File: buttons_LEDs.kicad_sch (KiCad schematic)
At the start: 6 parts, among them SW1 SW_Push, SW2 SW_Push

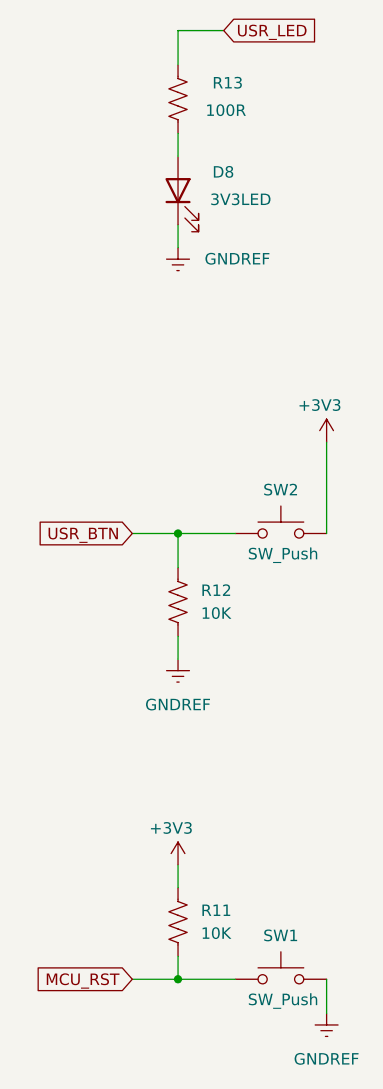
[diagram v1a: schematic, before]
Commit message: Completed design for digital outputs, tidied into own sheets and bussing for scalability
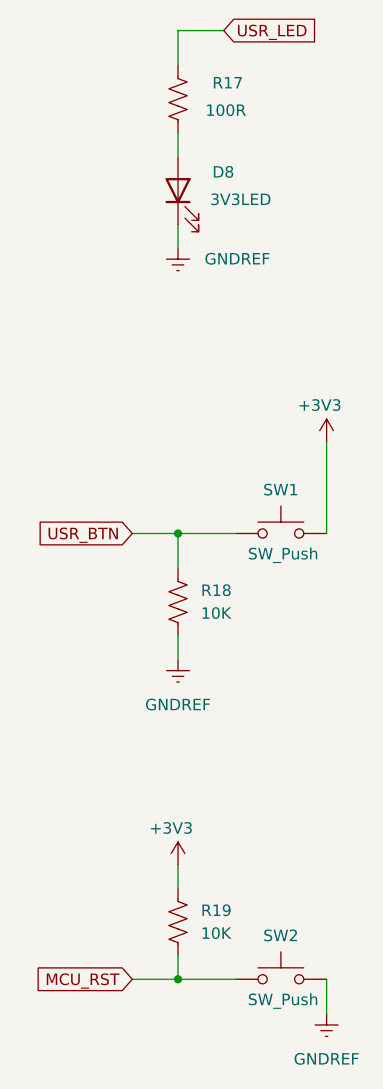
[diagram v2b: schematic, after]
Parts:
- renumbered R13 to R17, R12 to R18, R11 to R19, SW2 to SW1, SW1 to SW2
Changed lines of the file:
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@@
 		(on_board yes)
 		(dnp no)
-		(property "Reference" "#PWR0146"
+		(property "Reference" "#PWR0127"
 			(at 124.46 120.65 0)
 			(effects
@@
 			(project "Remora Nucleo F446ZE Hat"
 				(path "/5473abc6-7b93-43cc-a401-f691c4d7d7cf/e0f94f66-f67a-46dc-b55b-a3f70607aba8"
-					(reference "#PWR0146")
+					(reference "#PWR0127")
 					(unit 1)
 				)
@@
 		(on_board yes)
 		(dnp no)
-		(property "Reference" "SW2"
+		(property "Reference" "SW1"
 			(at 135.89 75.184 0)
 			(effects
@@
 			(project "Remora Nucleo F446ZE Hat"
 				(path "/5473abc6-7b93-43cc-a401-f691c4d7d7cf/e0f94f66-f67a-46dc-b55b-a3f70607aba8"
-					(reference "SW2")
+					(reference "SW1")
 					(unit 1)
 				)
@@
 		(dnp no)
 		(fields_autoplaced yes)
-		(property "Reference" "#PWR0149"
+		(property "Reference" "#PWR0126"
 			(at 124.46 100.33 0)
 			(effects
@@
 			(project "Remora Nucleo F446ZE Hat"
 				(path "/5473abc6-7b93-43cc-a401-f691c4d7d7cf/e0f94f66-f67a-46dc-b55b-a3f70607aba8"
-					(reference "#PWR0149")
+					(reference "#PWR0126")
 					(unit 1)
 				)
@@
 		(dnp no)
 		(fields_autoplaced yes)
-		(property "Reference" "R12"
+		(property "Reference" "R18"
 			(at 127 86.3599 0)
 			(effects
@@
 			(project "Remora Nucleo F446ZE Hat"
 				(path "/5473abc6-7b93-43cc-a401-f691c4d7d7cf/e0f94f66-f67a-46dc-b55b-a3f70607aba8"
-					(reference "R12")
+					(reference "R18")
 					(unit 1)
 				)
@@
 		(on_board yes)
 		(dnp no)
-		(property "Reference" "#PWR0148"
+		(property "Reference" "#PWR0128"
 			(at 140.97 73.66 0)
 			(effects
@@
 			(project "Remora Nucleo F446ZE Hat"
 				(path "/5473abc6-7b93-43cc-a401-f691c4d7d7cf/e0f94f66-f67a-46dc-b55b-a3f70607aba8"
-					(reference "#PWR0148")
+					(reference "#PWR0128")
 					(unit 1)
 				)
@@
 		(on_board yes)
 		(dnp no)
-		(property "Reference" "#PWR0151"
+		(property "Reference" "#PWR0125"
 			(at 124.46 54.61 0)
 			(effects
@@
 			(project "Remora Nucleo F446ZE Hat"
 				(path "/5473abc6-7b93-43cc-a401-f691c4d7d7cf/e0f94f66-f67a-46dc-b55b-a3f70607aba8"
-					(reference "#PWR0151")
+					(reference "#PWR0125")
 					(unit 1)
 				)
@@
 		(on_board yes)
 		(dnp no)
-		(property "Reference" "R13"
+		(property "Reference" "R17"
 			(at 128.27 29.972 0)
 			(effects
@@
 			(project "Remora Nucleo F446ZE Hat"
 				(path "/5473abc6-7b93-43cc-a401-f691c4d7d7cf/e0f94f66-f67a-46dc-b55b-a3f70607aba8"
-					(reference "R13")
+					(reference "R17")
 					(unit 1)
 				)
@@
 		(dnp no)
 		(fields_autoplaced yes)
-		(property "Reference" "R11"
+		(property "Reference" "R19"
 			(at 127 121.9199 0)
 			(effects
@@
 			(project "Remora Nucleo F446ZE Hat"
 				(path "/5473abc6-7b93-43cc-a401-f691c4d7d7cf/e0f94f66-f67a-46dc-b55b-a3f70607aba8"
-					(reference "R11")
+					(reference "R19")
 					(unit 1)
 				)
@@
 		(on_board yes)
 		(dnp no)
-		(property "Reference" "SW1"
+		(property "Reference" "SW2"
 			(at 135.89 124.714 0)
 			(effects
@@
 			(project "Remora Nucleo F446ZE Hat"
 				(path "/5473abc6-7b93-43cc-a401-f691c4d7d7cf/e0f94f66-f67a-46dc-b55b-a3f70607aba8"
-					(reference "SW1")
+					(reference "SW2")
 					(unit 1)
 				)
@@
 		(dnp no)
 		(fields_autoplaced yes)
-		(property "Reference" "#PWR0147"
+		(property "Reference" "#PWR0129"
 			(at 140.97 139.7 0)
 			(effects
@@
 			(project "Remora Nucleo F446ZE Hat"
 				(path "/5473abc6-7b93-43cc-a401-f691c4d7d7cf/e0f94f66-f67a-46dc-b55b-a3f70607aba8"
-					(reference "#PWR0147")
-					(unit 1)
-				)
+					(reference "#PWR0129")
+					(unit 1)
+				)

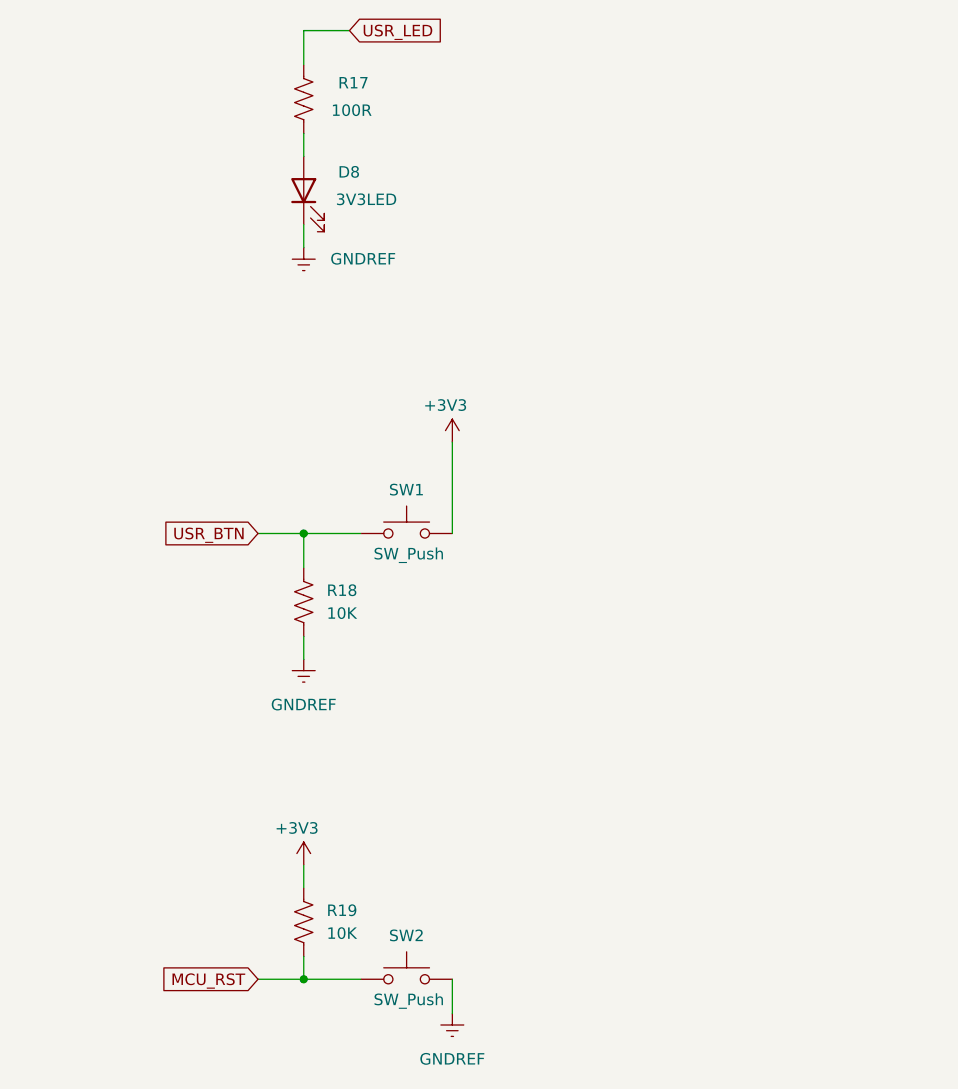
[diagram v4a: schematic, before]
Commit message: Fixed bug with lack of pin header for CN11 and CN12. Addeded RPI header and aligned it, assigned some safe footprints
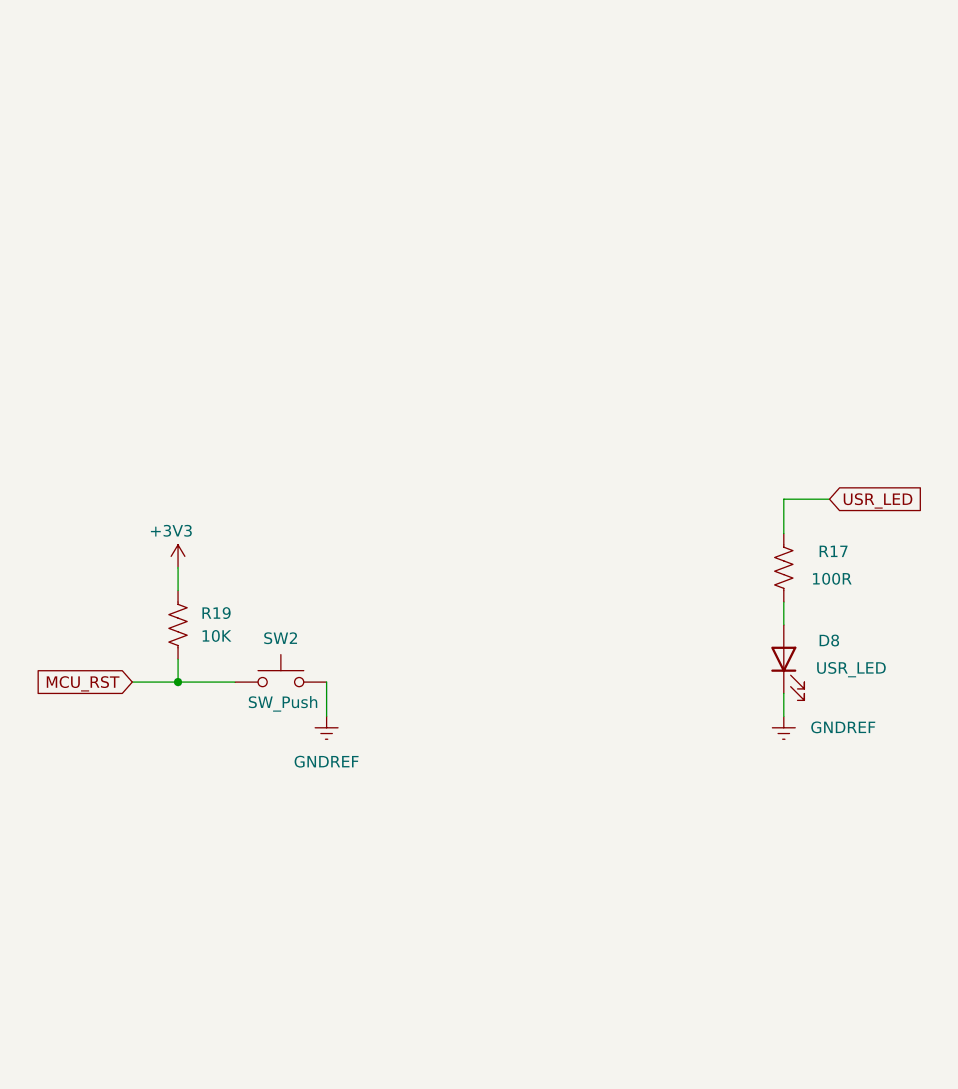
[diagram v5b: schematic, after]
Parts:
- removed R18: 10K, symbol Device:R_US
- removed SW1: SW_Push, symbol Switch:SW_Push
- D8: value 3V3LED -> USR_LED
- R19: footprint (none) -> Resistor_SMD:R_1206_3216Metric_Pad1.30x1.75mm_HandSolder
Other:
- moved on the sheet: D8, R17, R19, SW2

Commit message: updates to read me, marked V1 parts inactive and made start on board layout for initial test board. fixes to BOM to suit
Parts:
- SW2: footprint (none) -> Button_Switch_SMD:SW_SPST_Omron_B3FS-100xP
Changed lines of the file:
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@@
 			)
 		)
-		(property "Footprint" ""
+		(property "Footprint" "Button_Switch_SMD:SW_SPST_Omron_B3FS-100xP"
 			(at 121.92 91.44 0)
 			(effects
